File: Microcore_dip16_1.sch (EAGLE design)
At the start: 17 parts, among them IC1 74LS595N, IC2 7459716DIP

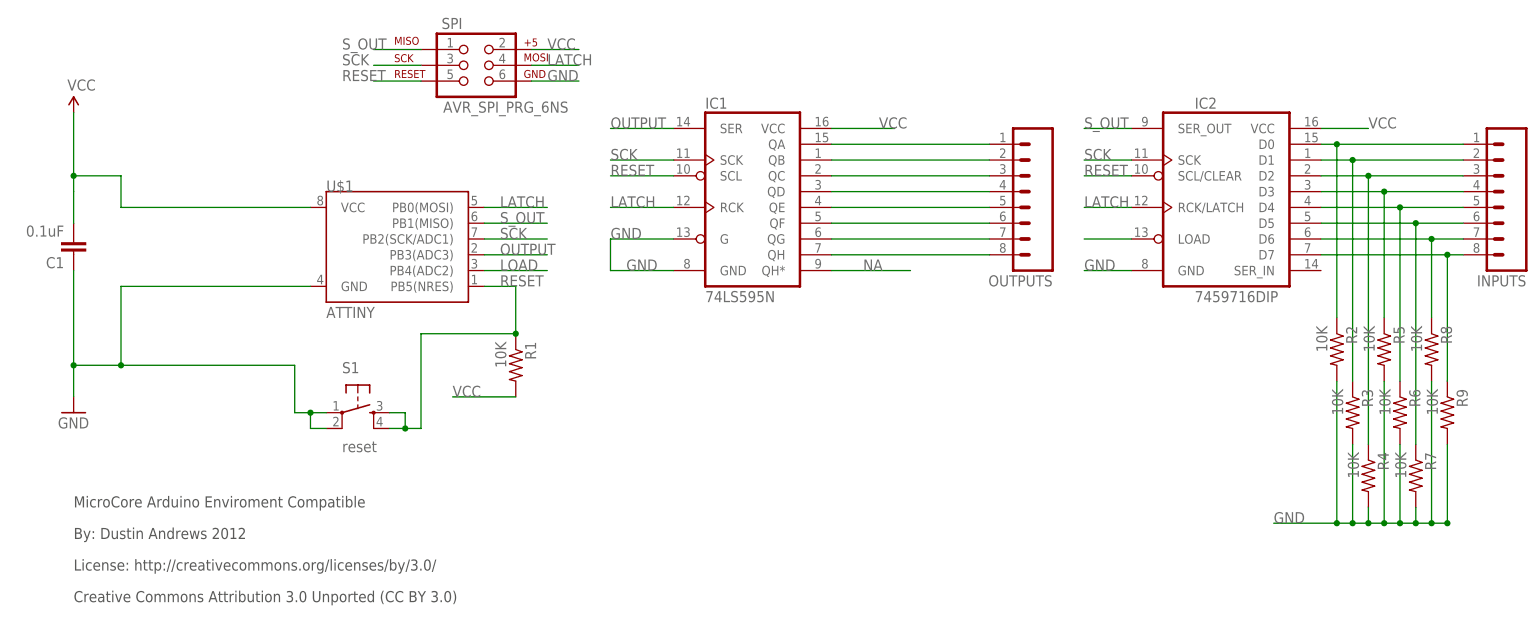
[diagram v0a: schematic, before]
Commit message: Added resistor array and power regulator
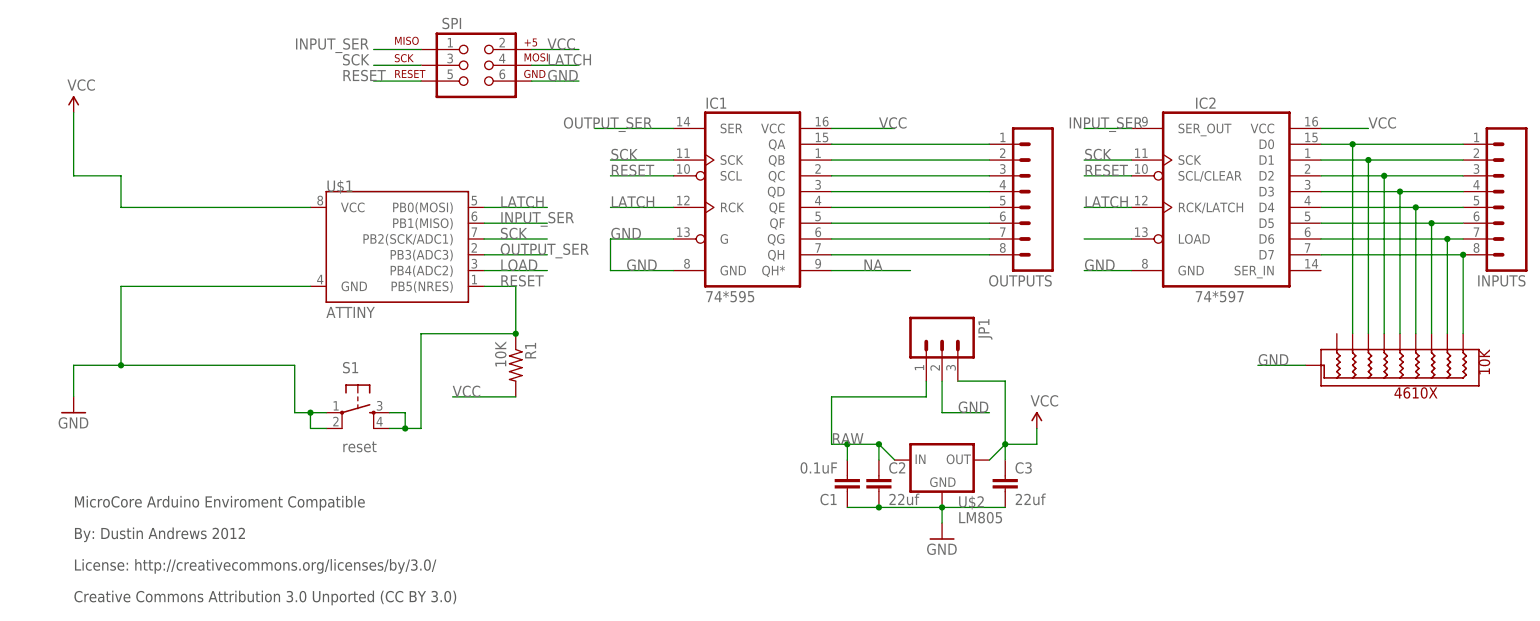
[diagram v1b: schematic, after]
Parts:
- removed R2, R3, R4, R5, R6, R7, R8, R9: 10K, SparkFun:RESISTORPTH-1/4W
- added 10K: 4610X, Dustin:4610X
- added C2, C3: 22uf, SparkFun:CAPPTH
- added JP1: (no value), SparkFun:M03PTH
- added U$2: LM805, SparkFun:V_REG_78XXSINK
- IC1: value 74LS595N -> 74*595
- IC2: value 7459716DIP -> 74*597
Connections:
- net OUTPUT renamed OUTPUT_SER
- net S_OUT renamed INPUT_SER
- new net RAW: C1.2, C2.1, JP1.1, U$2.IN
- net GND: now also 10K.GND, C2.2, C3.2, JP1.2, U$2.GND; no longer R2.2, R3.2, R4.2, R5.2, R6.2, R7.2, R8.2, R9.2
- net N$10: now also 10K.3; no longer R3.1
- net N$11: now also 10K.4; no longer R4.1
- net N$12: now also 10K.5; no longer R5.1
- net N$13: now also 10K.6; no longer R6.1
- net N$14: now also 10K.7; no longer R7.1
- net N$15: now also 10K.8; no longer R8.1
- net N$16: now also 10K.9; no longer R9.1
- net N$9: now also 10K.2; no longer R2.1
- net VCC: now also C3.1, JP1.3, U$2.OUT; no longer C1.2
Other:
- moved on the sheet: C1
